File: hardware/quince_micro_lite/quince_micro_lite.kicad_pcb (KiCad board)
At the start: 4 copper layers, 21 x 51 mm, 46 parts, among them J1 Conn_01x04_Pin, J11 Conn_01x20_Pin, J12 Conn_01x20_Pin, J21 Conn_01x05_Pin, J22 Conn_01x05_Pin, J30 USB_C_Receptacle_USB2.0_14P, J40 Conn_01x10, J50 Micro_SD_Card, U1 CH32V305RBT6, U30 ME6211C33M5, U40 XC6206P-2V8MR, U50 TJA1042TK-3, Y100 12MHz SMD2520

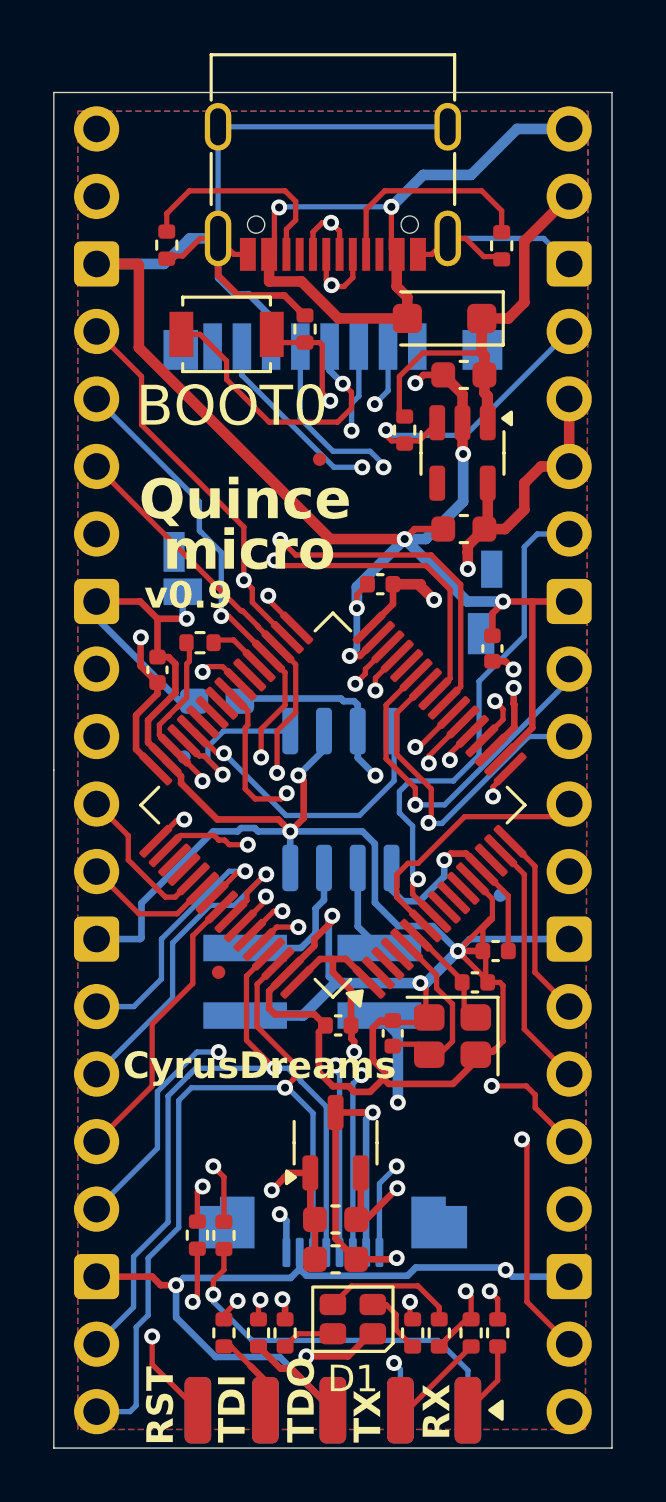
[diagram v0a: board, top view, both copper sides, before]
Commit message: version 1.0 commit, changed PB8 and PB9, added 5V and 3.3V supply to debug connector
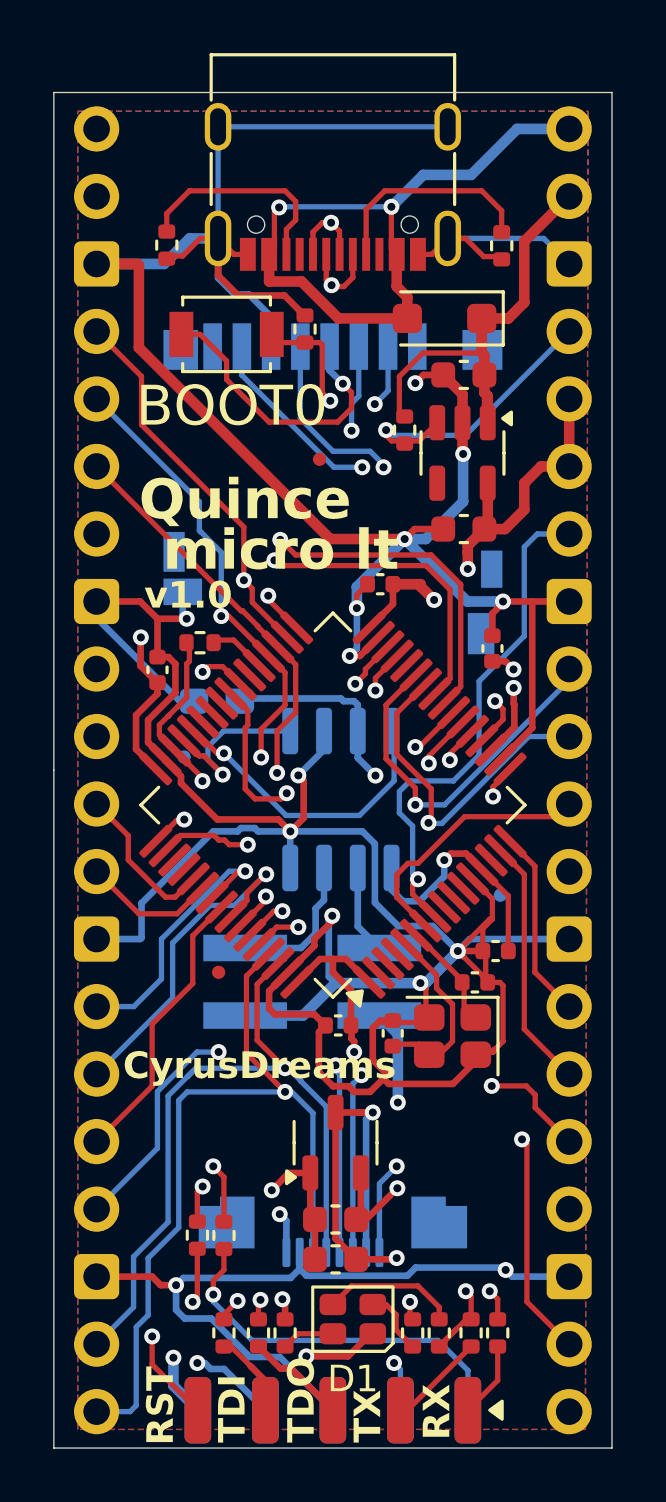
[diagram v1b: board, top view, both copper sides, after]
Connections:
- J22 pad 1: unconnected-(J22-Pin_1-Pad1) -> +5V
- J22 pad 2: unconnected-(J22-Pin_2-Pad2) -> +3V3
- U1 pad 61: LCD_RS -> LCD_RES_B
- U1 pad 62: LCD_RES_B -> LCD_RS
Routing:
- net +5V: track 68.5 -> 86.7 mm, vias 2 -> 3
- net +3V3: track 136.6 -> 144.1 mm, vias 11 -> 12
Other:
- board text added: "micro lt"
- board text added: "v1.0"
- board text removed: "micro"
- board text removed: "v0.9"
